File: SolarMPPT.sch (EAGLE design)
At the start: 40 parts, among them J1 CORTEX_DEBUG_SMD, U1 STM32F091CCT6, U3 LTC1155, U4 LM22674MRX-5.0, U5 3.3V

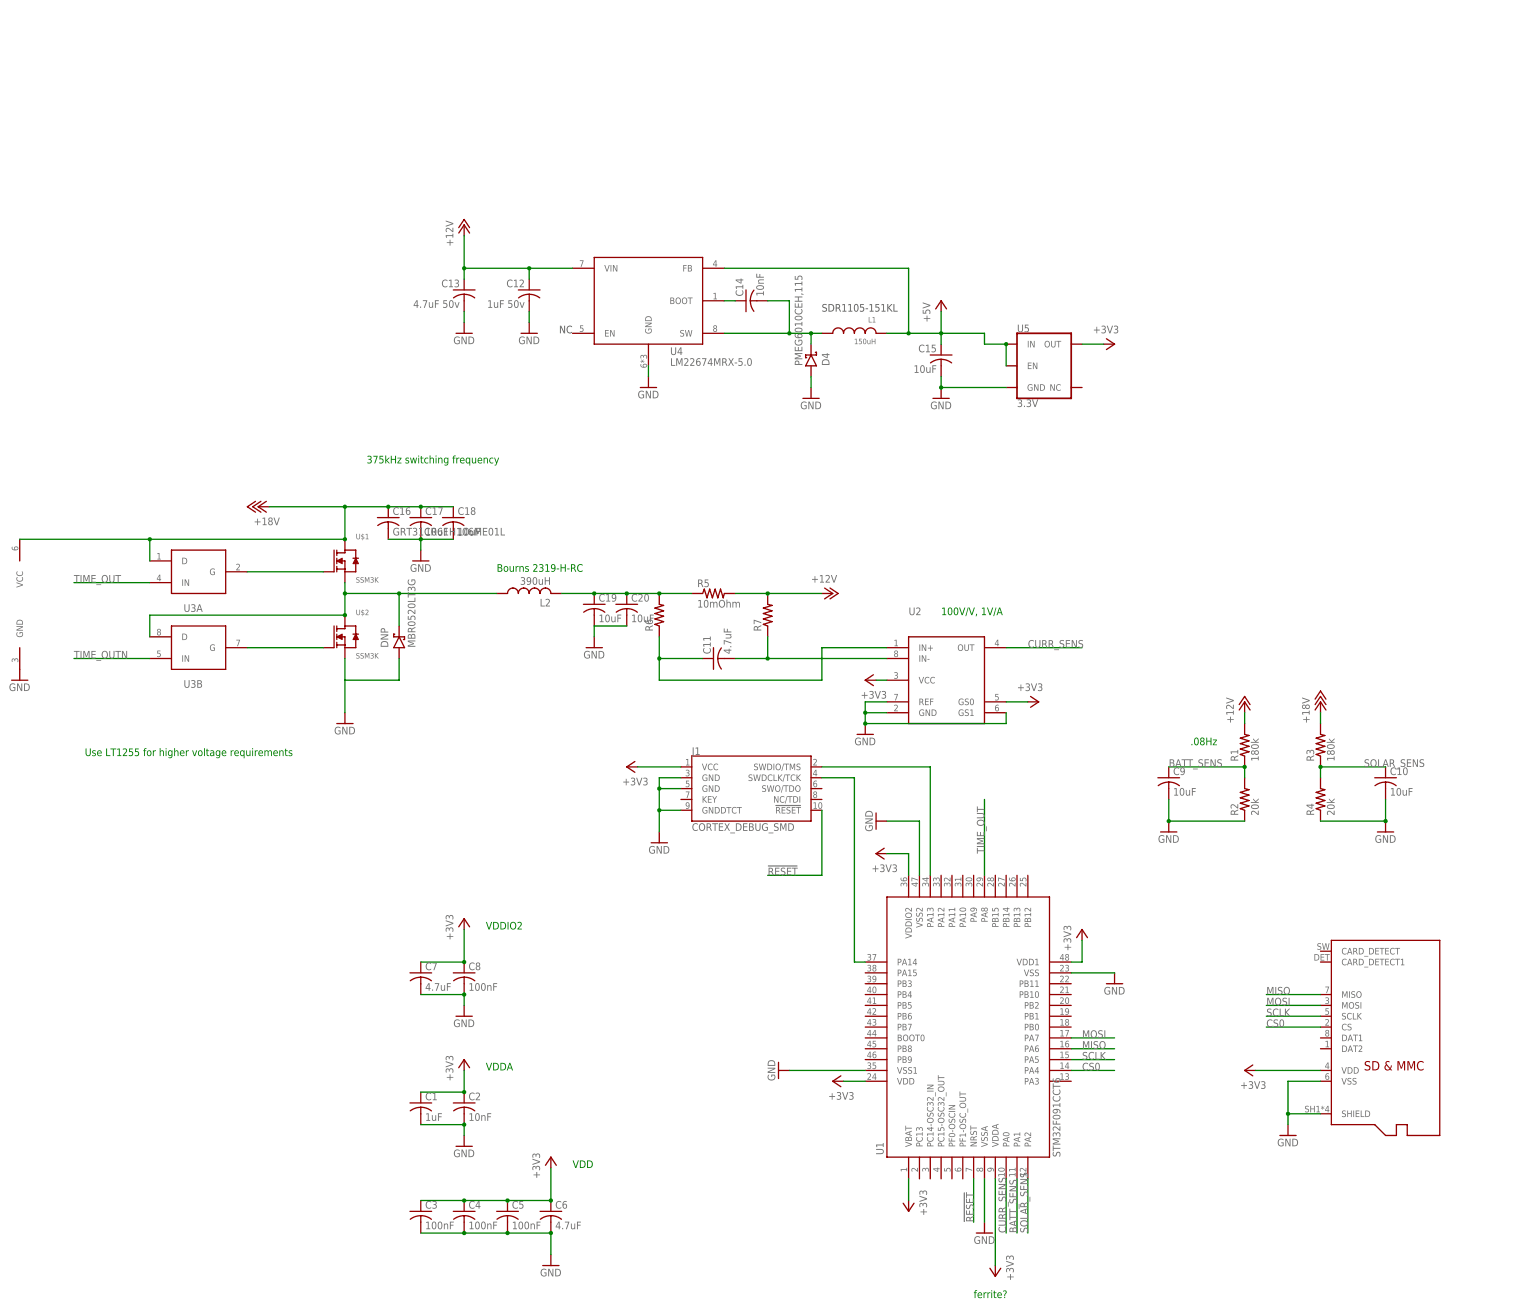
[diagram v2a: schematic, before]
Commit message: Added decoupling caps, cleaned up schematic, ready for review
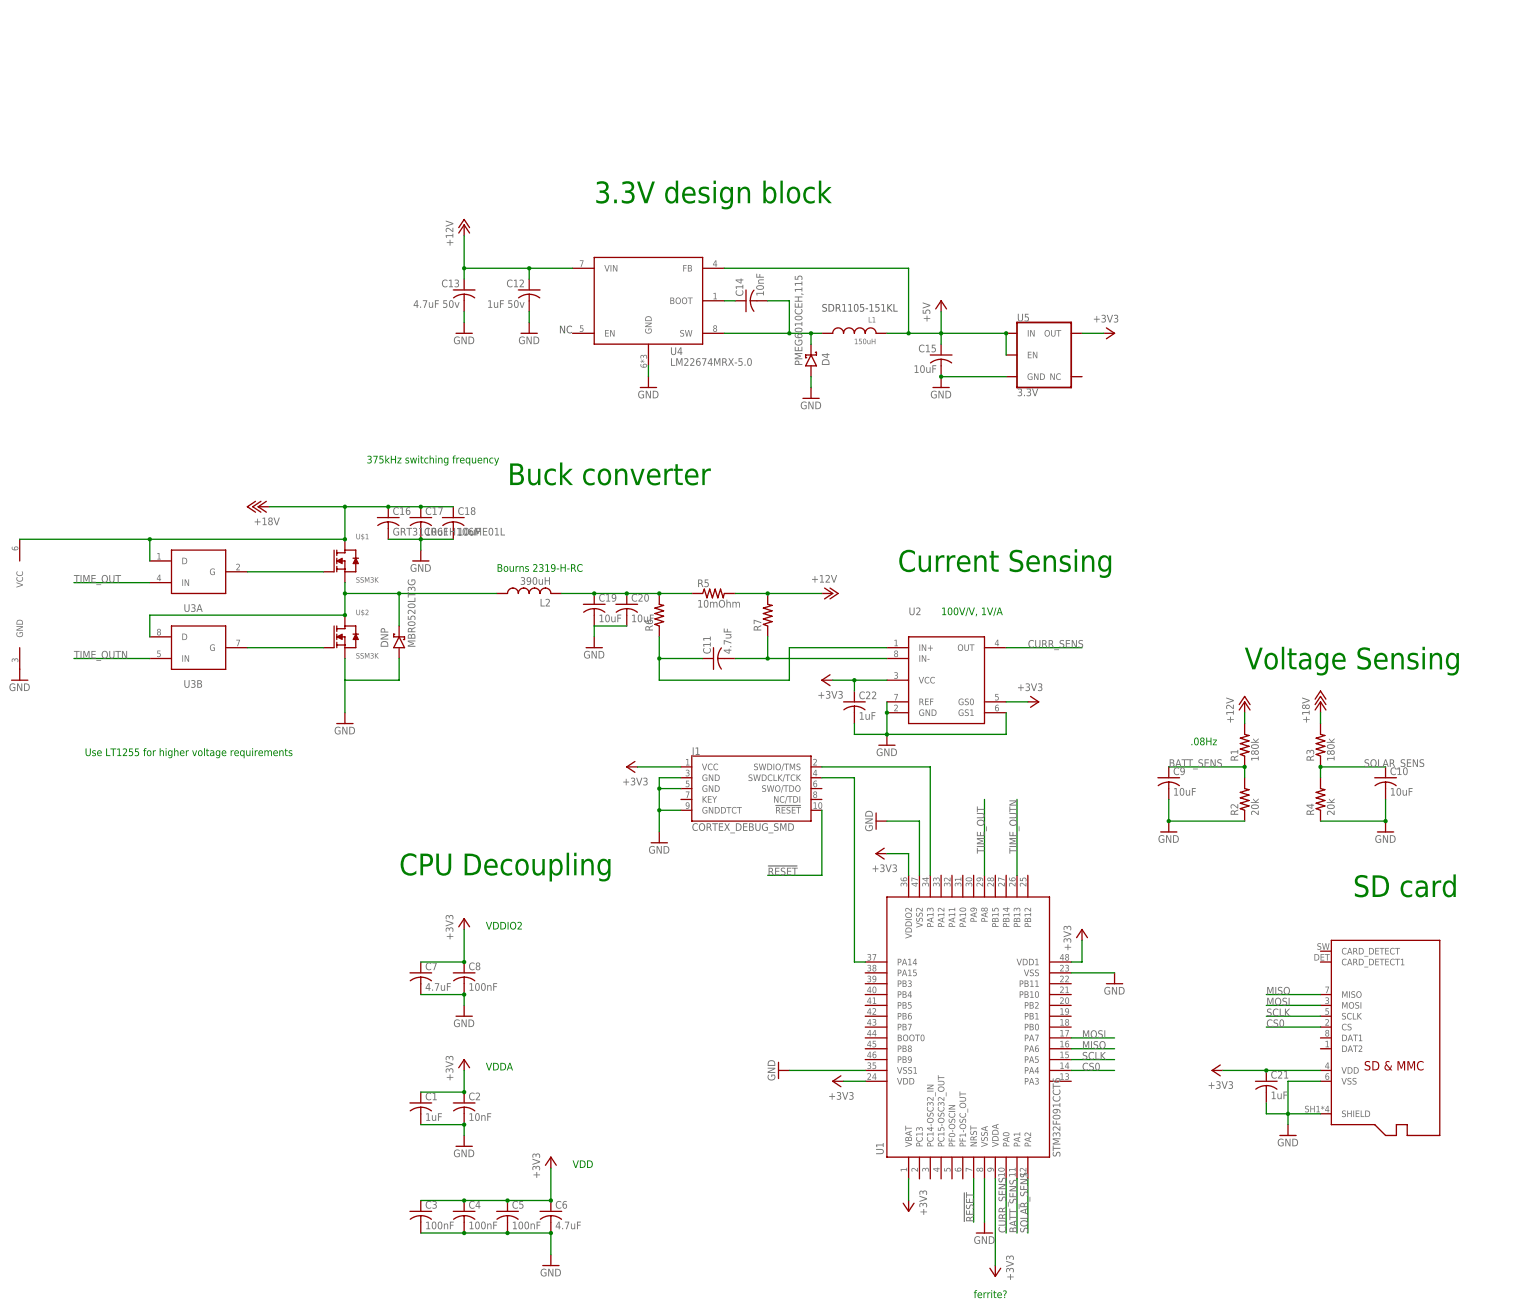
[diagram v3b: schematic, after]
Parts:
- added C21, C22: 1uF, rcl:C-USC0805
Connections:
- net +3V3: now also C21.1, C22.1
- net GND: now also C21.2, C22.2
- net TIME_OUTN: now also U1.PB13
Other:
- note added: "3.3V design block"
- note added: "Buck converter"
- note added: "CPU Decoupling"
- note added: "Current Sensing"
- note added: "SD card"
- note added: "Voltage Sensing"
- moved on the sheet: U5
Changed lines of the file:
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@@
 <part name="GND21" library="supply1" library_urn="urn:adsk.eagle:library:371" deviceset="GND" device=""/>
 <part name="DNP" library="FormE" deviceset="MBR0520LT3G" device="" value="MBR0520LT3G"/>
+<part name="C21" library="rcl" library_urn="urn:adsk.eagle:library:334" deviceset="C-US" device="C0805" package3d_urn="urn:adsk.eagle:package:23617/2" value="1uF"/>
+<part name="C22" library="rcl" library_urn="urn:adsk.eagle:library:334" deviceset="C-US" device="C0805" package3d_urn="urn:adsk.eagle:package:23617/2" value="1uF"/>
 </parts>
 <sheets>
@@
 <text x="-187.96" y="129.54" size="1.778" layer="91">Use LT1255 for higher voltage requirements</text>
 <text x="-91.44" y="172.72" size="1.778" layer="91">Bourns 2319-H-RC</text>
+<text x="83.82" y="149.86" size="5.08" layer="91">Voltage Sensing</text>
+<text x="2.54" y="172.72" size="5.08" layer="91">Current Sensing</text>
+<text x="-114.3" y="101.6" size="5.08" layer="91">CPU Decoupling</text>
+<text x="-68.58" y="259.08" size="5.08" layer="91">3.3V design block</text>
+<text x="-88.9" y="193.04" size="5.08" layer="91">Buck converter</text>
+<text x="109.22" y="96.52" size="5.08" layer="91">SD card</text>
 </plain>
 <instances>
@@
 <attribute name="VALUE" x="-55.88" y="124.46" size="1.778" layer="96" rot="R180"/>
 </instance>
-<instance part="+3V6" gate="G$1" x="83.82" y="55.88" smashed="yes" rot="R90">
-<attribute name="VALUE" x="88.9" y="53.34" size="1.778" layer="96" rot="R180"/>
+<instance part="+3V6" gate="G$1" x="76.2" y="55.88" smashed="yes" rot="R90">
+<attribute name="VALUE" x="81.28" y="53.34" size="1.778" layer="96" rot="R180"/>
 </instance>
 <instance part="GND2" gate="1" x="22.86" y="17.78" smashed="yes">
@@
 <attribute name="VALUE" x="5.08" y="160.02" size="1.778" layer="96"/>
 </instance>
-<instance part="+3V11" gate="G$1" x="-5.08" y="147.32" smashed="yes" rot="R90">
-<attribute name="VALUE" x="0" y="144.78" size="1.778" layer="96" rot="R180"/>
-</instance>
-<instance part="GND12" gate="1" x="-5.08" y="134.62" smashed="yes">
-<attribute name="VALUE" x="-7.62" y="132.08" size="1.778" layer="96"/>
+<instance part="+3V11" gate="G$1" x="-15.24" y="147.32" smashed="yes" rot="R90">
+<attribute name="VALUE" x="-10.16" y="144.78" size="1.778" layer="96" rot="R180"/>
+</instance>
+<instance part="GND12" gate="1" x="0" y="132.08" smashed="yes">
+<attribute name="VALUE" x="-2.54" y="129.54" size="1.778" layer="96"/>
 </instance>
 <instance part="+3V12" gate="G$1" x="35.56" y="142.24" smashed="yes" rot="R270">
@@
 <attribute name="VALUE" x="11.684" y="219.329" size="1.778" layer="96" rot="MR0"/>
 </instance>
-<instance part="GND20" gate="1" x="12.7" y="213.36" smashed="yes">
-<attribute name="VALUE" x="10.16" y="210.82" size="1.778" layer="96"/>
-</instance>
-<instance part="U5" gate="G$1" x="38.1" y="220.98" smashed="yes">
-<attribute name="NAME" x="30.48" y="228.854" size="1.778" layer="95" font="vector"/>
-<attribute name="VALUE" x="30.48" y="213.106" size="1.778" layer="96" font="vector" align="top-left"/>
-</instance>
-<instance part="+3V13" gate="G$1" x="53.34" y="226.06" smashed="yes" rot="R270">
-<attribute name="VALUE" x="48.26" y="228.6" size="1.778" layer="96"/>
+<instance part="GND20" gate="1" x="12.7" y="215.9" smashed="yes">
+<attribute name="VALUE" x="10.16" y="213.36" size="1.778" layer="96"/>
+</instance>
+<instance part="U5" gate="G$1" x="38.1" y="223.52" smashed="yes">
+<attribute name="NAME" x="30.48" y="231.394" size="1.778" layer="95" font="vector"/>
+<attribute name="VALUE" x="30.48" y="215.646" size="1.778" layer="96" font="vector" align="top-left"/>
+</instance>
+<instance part="+3V13" gate="G$1" x="53.34" y="228.6" smashed="yes" rot="R270">
+<attribute name="VALUE" x="48.26" y="231.14" size="1.778" layer="96"/>
 </instance>
 <instance part="P+5" gate="1" x="-99.06" y="254" smashed="yes">
@@
 <attribute name="NAME" x="-116.84" y="154.94" size="1.778" layer="95" rot="R90"/>
 <attribute name="VALUE" x="-110.49" y="154.94" size="1.778" layer="96" rot="R90"/>
+</instance>
+<instance part="C21" gate="G$1" x="88.9" y="53.34" smashed="yes">
+<attribute name="NAME" x="89.916" y="53.975" size="1.778" layer="95"/>
+<attribute name="VALUE" x="89.916" y="49.149" size="1.778" layer="96"/>
+</instance>
+<instance part="C22" gate="G$1" x="-7.62" y="142.24" smashed="yes">
+<attribute name="NAME" x="-6.604" y="142.875" size="1.778" layer="95"/>
+<attribute name="VALUE" x="-6.604" y="138.049" size="1.778" layer="96"/>
 </instance>
 </instances>
@@
 <wire x1="101.6" y1="45.72" x2="93.98" y2="45.72" width="0.1524" layer="91"/>
 <junction x="93.98" y="45.72"/>
+<pinref part="C21" gate="G$1" pin="2"/>
+<wire x1="88.9" y1="48.26" x2="88.9" y2="45.72" width="0.1524" layer="91"/>
+<wire x1="88.9" y1="45.72" x2="93.98" y2="45.72" width="0.1524" layer="91"/>
 </segment>
 <segment>
@@
 <pinref part="GND12" gate="1" pin="GND"/>
 <pinref part="U2" gate="G$1" pin="GND"/>
-<wire x1="-5.08" y1="137.16" x2="-5.08" y2="139.7" width="0.1524" layer="91"/>
-<wire x1="-5.08" y1="139.7" x2="0" y2="139.7" width="0.1524" layer="91"/>
+<wire x1="0" y1="134.62" x2="0" y2="139.7" width="0.1524" layer="91"/>
 <pinref part="U2" gate="G$1" pin="REF"/>
-<wire x1="0" y1="142.24" x2="-5.08" y2="142.24" width="0.1524" layer="91"/>
-<wire x1="-5.08" y1="142.24" x2="-5.08" y2="139.7" width="0.1524" layer="91"/>
-<junction x="-5.08" y="139.7"/>
+<wire x1="0" y1="142.24" x2="0" y2="139.7" width="0.1524" layer="91"/>
+<junction x="0" y="139.7"/>
 <pinref part="U2" gate="G$1" pin="GS1"/>
-<wire x1="27.94" y1="139.7" x2="27.94" y2="137.16" width="0.1524" layer="91"/>
-<wire x1="27.94" y1="137.16" x2="-5.08" y2="137.16" width="0.1524" layer="91"/>
-<junction x="-5.08" y="137.16"/>
+<wire x1="27.94" y1="139.7" x2="27.94" y2="134.62" width="0.1524" layer="91"/>
+<wire x1="27.94" y1="134.62" x2="0" y2="134.62" width="0.1524" layer="91"/>
+<junction x="0" y="134.62"/>
+<pinref part="C22" gate="G$1" pin="2"/>
+<wire x1="-7.62" y1="137.16" x2="-7.62" y2="134.62" width="0.1524" layer="91"/>
+<wire x1="-7.62" y1="134.62" x2="0" y2="134.62" width="0.1524" layer="91"/>
 </segment>
 <segment>
@@
 <pinref part="GND20" gate="1" pin="GND"/>
 <pinref part="C15" gate="G$1" pin="2"/>
-<wire x1="12.7" y1="215.9" x2="12.7" y2="218.44" width="0.1524" layer="91"/>
 <pinref part="U5" gate="G$1" pin="GND"/>
-<wire x1="27.94" y1="215.9" x2="12.7" y2="215.9" width="0.1524" layer="91"/>
-<junction x="12.7" y="215.9"/>
+<wire x1="27.94" y1="218.44" x2="12.7" y2="218.44" width="0.1524" layer="91"/>
+<junction x="12.7" y="218.44"/>
 </segment>
 <segment>
@@
 <pinref part="+3V6" gate="G$1" pin="+3V3"/>
 <pinref part="H1" gate="G$1" pin="VDD"/>
-<wire x1="86.36" y1="55.88" x2="101.6" y2="55.88" width="0.1524" layer="91"/>
+<wire x1="78.74" y1="55.88" x2="88.9" y2="55.88" width="0.1524" layer="91"/>
+<pinref part="C21" gate="G$1" pin="1"/>
+<wire x1="88.9" y1="55.88" x2="101.6" y2="55.88" width="0.1524" layer="91"/>
+<junction x="88.9" y="55.88"/>
 </segment>
 <segment>
@@
 <pinref part="+3V11" gate="G$1" pin="+3V3"/>
 <pinref part="U2" gate="G$1" pin="VCC"/>
-<wire x1="-2.54" y1="147.32" x2="0" y2="147.32" width="0.1524" layer="91"/>
+<wire x1="-12.7" y1="147.32" x2="-7.62" y2="147.32" width="0.1524" layer="91"/>
+<pinref part="C22" gate="G$1" pin="1"/>
+<wire x1="-7.62" y1="147.32" x2="0" y2="147.32" width="0.1524" layer="91"/>
+<wire x1="-7.62" y1="144.78" x2="-7.62" y2="147.32" width="0.1524" layer="91"/>
+<junction x="-7.62" y="147.32"/>
 </segment>
 <segment>
@@
 <pinref part="U5" gate="G$1" pin="OUT"/>
 <pinref part="+3V13" gate="G$1" pin="+3V3"/>
-<wire x1="45.72" y1="226.06" x2="50.8" y2="226.06" width="0.1524" layer="91"/>
+<wire x1="45.72" y1="228.6" x2="50.8" y2="228.6" width="0.1524" layer="91"/>
 </segment>
 </net>
@@
 <wire x1="-53.34" y1="152.4" x2="-43.18" y2="152.4" width="0.1524" layer="91"/>
 <pinref part="U2" gate="G$1" pin="IN+"/>
-<wire x1="0" y1="154.94" x2="-15.24" y2="154.94" width="0.1524" layer="91"/>
-<wire x1="-15.24" y1="154.94" x2="-15.24" y2="147.32" width="0.1524" layer="91"/>
-<wire x1="-15.24" y1="147.32" x2="-53.34" y2="147.32" width="0.1524" layer="91"/>
+<wire x1="0" y1="154.94" x2="-22.86" y2="154.94" width="0.1524" layer="91"/>
+<wire x1="-22.86" y1="154.94" x2="-22.86" y2="147.32" width="0.1524" layer="91"/>
+<wire x1="-22.86" y1="147.32" x2="-53.34" y2="147.32" width="0.1524" layer="91"/>
 <wire x1="-53.34" y1="147.32" x2="-53.34" y2="152.4" width="0.1524" layer="91"/>
 <junction x="-53.34" y="152.4"/>
@@
 <wire x1="12.7" y1="228.6" x2="12.7" y2="226.06" width="0.1524" layer="91"/>
 <pinref part="U5" gate="G$1" pin="EN"/>
-<wire x1="22.86" y1="226.06" x2="27.94" y2="226.06" width="0.1524" layer="91"/>
-<wire x1="27.94" y1="226.06" x2="27.94" y2="220.98" width="0.1524" layer="91"/>
-<junction x="27.94" y="226.06"/>
-<wire x1="12.7" y1="228.6" x2="22.86" y2="228.6" width="0.1524" layer="91"/>
-<wire x1="22.86" y1="228.6" x2="22.86" y2="226.06" width="0.1524" layer="91"/>
+<wire x1="27.94" y1="228.6" x2="27.94" y2="223.52" width="0.1524" layer="91"/>
+<junction x="27.94" y="228.6"/>
+<wire x1="12.7" y1="228.6" x2="27.94" y2="228.6" width="0.1524" layer="91"/>
 </segment>
 </net>
@@
 <label x="-190.5" y="152.4" size="1.778" layer="95"/>
 </segment>
-</net>
+<segment>
+<pinref part="U1" gate="G$1" pin="PB13"/>
+<wire x1="30.48" y1="101.6" x2="30.48" y2="119.38" width="0.1524" layer="91"/>
+<label x="30.48" y="106.68" size="1.778" layer="95" rot="R90"/>
+</segment>
+</net>
